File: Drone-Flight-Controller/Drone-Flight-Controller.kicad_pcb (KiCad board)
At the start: 2 copper layers, 30 x 65 mm, 45 parts, among them J1 Screw_Terminal_01x02, J10 TestPoint, J11 TestPoint, J12 TestPoint, J2 Raspberry_Pi_4, J3 TestPoint, J4 TestPoint, J5 TestPoint, J6 TestPoint, J7 TestPoint, J8 TestPoint, J9 TestPoint, SW1 SW_Omron_B3FS, U1 MCP1700x-180xxMB, U2 LMR51430, U3 ADC101C021CIMK, U4 ICM-20948, U5 BMP280, U6 PCA9531PW

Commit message: move imu to center of pcb
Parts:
- moved U4 7.45 mm to (27.2, 44.6)
- moved C2 7.15 mm to (23.6, 38.6)
- moved C3 7.15 mm to (23.6, 40.6)
- moved U1 7.15 mm to (27.0, 39.6)
- moved C7 7.07 mm to (25.0, 47.8), turned to -90 degrees
- moved C6 6.61 mm to (24.0, 43.2)
- moved C9 6.61 mm to (24.0, 47.2)
- moved R7 6.61 mm to (24.0, 45.2)
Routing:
- net +5V: track 73.4 -> 39.9 mm, vias 11 -> 18
- net +3.3V: track 79.4 -> 61.8 mm
- net +1V8: track 10.8 -> 4.61 mm
- net GND: track 5.39 -> 1.42 mm, vias 17 -> 14
- net I2C_SCL: track 75.3 -> 77.9 mm, vias 3 -> 5
- net I2C_SDA: track 74.2 -> 76.0 mm
- net Net-(U4-REGOUT): track 1.77 -> 2.79 mm
- net Net-(U4-SDO/AD0): track 1.47 -> 2.47 mm
- added copper zone on F.Cu, net +3.3V
- added copper zone on B.Cu, net +5V
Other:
- board text added: "DO NOT COVER"
- board text added: "imu"
- board text removed: "gyro"

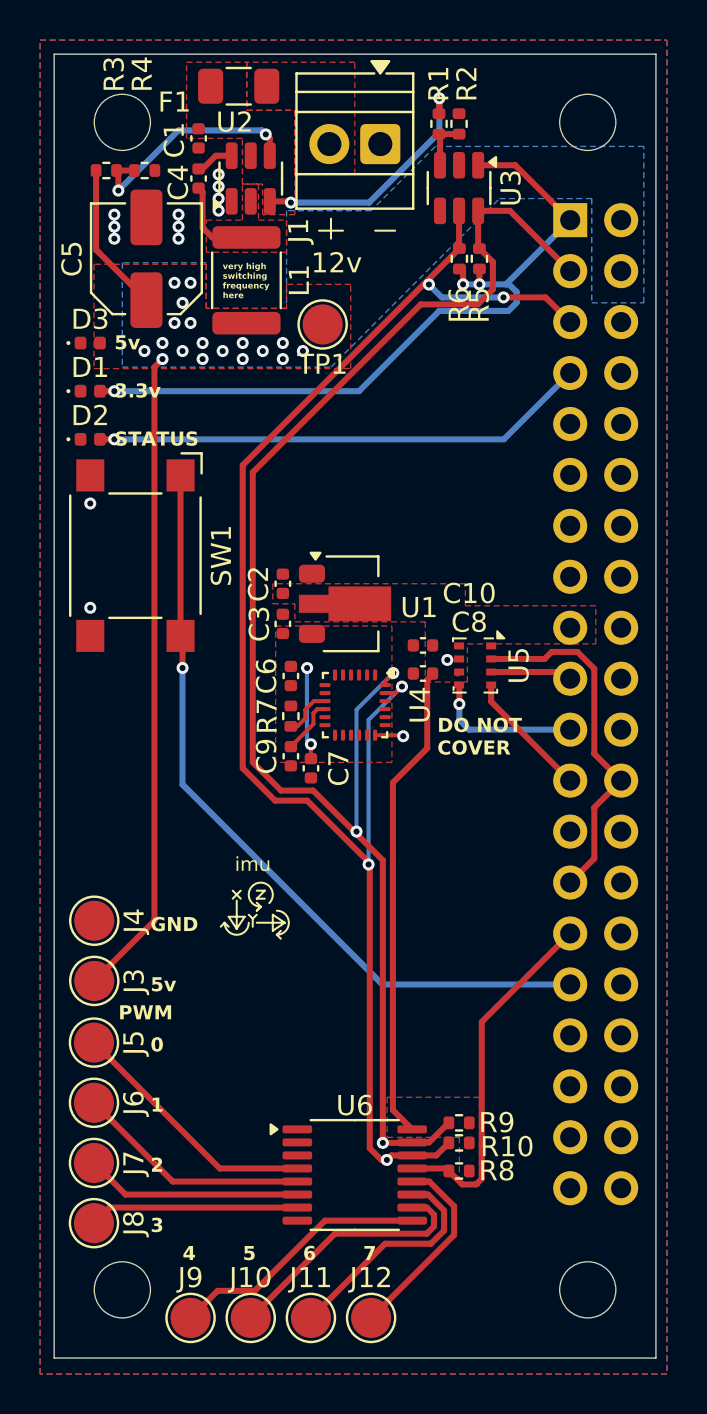
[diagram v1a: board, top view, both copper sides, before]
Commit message: added imu level shifter
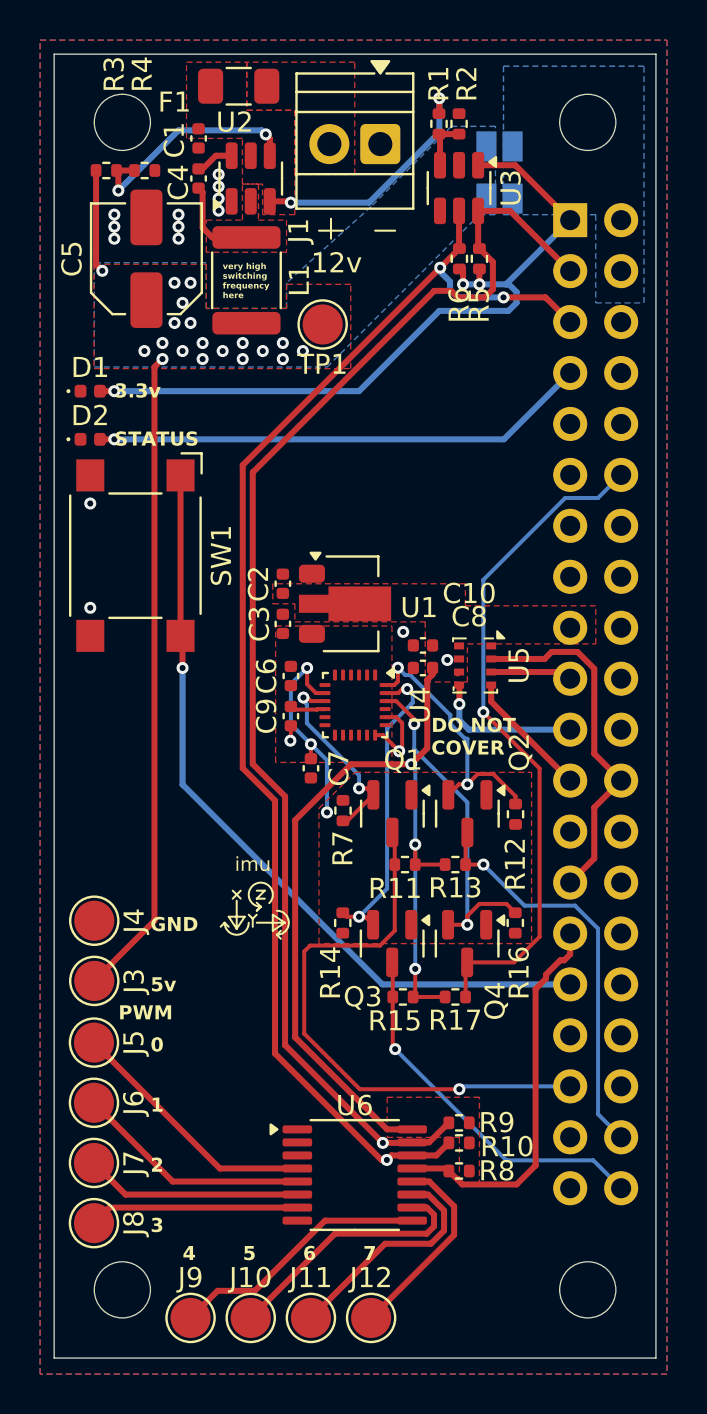
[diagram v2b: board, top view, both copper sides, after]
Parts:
- removed D3: LED, LED_SMD:LED_0402_1005Metric
- added JP1: SolderJumper_2_Open, Jumper:SolderJumper-2_P1.3mm_Open_Pad1.0x1.5mm, B.Cu at (34.4, 16.8)
- added JP2: SolderJumper_2_Open, Jumper:SolderJumper-2_P1.3mm_Open_Pad1.0x1.5mm, B.Cu at (34.4, 19.4)
- added Q1: BSS138, Package_TO_SOT_SMD:SOT-23, F.Cu at (29.1, 50.1)
- added Q2: BSS138, Package_TO_SOT_SMD:SOT-23, F.Cu at (32.8, 50.1)
- added Q3: BSS138, Package_TO_SOT_SMD:SOT-23, F.Cu at (29.1, 56.5)
- added Q4: BSS138, Package_TO_SOT_SMD:SOT-23, F.Cu at (32.8, 56.5)
- added R11: 10kOhm, Resistor_SMD:R_0402_1005Metric, F.Cu at (29.7, 52.6)
- added R12: 10kOhm, Resistor_SMD:R_0402_1005Metric, F.Cu at (35.2, 50.1)
- added R13: 10kOhm, Resistor_SMD:R_0402_1005Metric, F.Cu at (32.2, 52.6)
- added R14: 10kOhm, Resistor_SMD:R_0402_1005Metric, F.Cu at (26.6, 55.5)
- added R15: 10kOhm, Resistor_SMD:R_0402_1005Metric, F.Cu at (29.6, 59.2)
- added R16: 10kOhm, Resistor_SMD:R_0402_1005Metric, F.Cu at (35.2, 55.5)
- added R17: 10kOhm, Resistor_SMD:R_0402_1005Metric, F.Cu at (32.2, 59.2)
- moved R7 5.38 mm to (26.6, 49.9)
- moved C9 2.00 mm to (24.0, 45.2)
- moved C8 0.28 mm to (30.6, 42.8)
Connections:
- net Net-(U4-SDO/AD0) renamed IMU_SDO_LV
- J2 pad 12: unconnected-(J2-GPIO18/SPI1_~{CE0}/PCM_CLK/PWM0-Pad12) -> IMU_CS_HV
- J2 pad 35: unconnected-(J2-GPIO19/SPI1_MISO/PCM_FS-Pad35) -> IMU_SDO_HV
- J2 pad 38: unconnected-(J2-GPIO20/SPI1_MOSI/PCM_DIN/PWM1-Pad38) -> IMU_SDI_HV
- J2 pad 40: unconnected-(J2-GPIO21/SPI1_SCLK/PCM_DOUT-Pad40) -> IMU_SCL_HV
- U4 pad 22: unconnected-(U4-~{CS}-Pad22) -> IMU_CS_LV
- U4 pad 23: I2C_SCL -> IMU_SCL_LV
- U4 pad 24: I2C_SDA -> IMU_SDI_LV
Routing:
- net IMU_CS_HV: track 0.00 -> 33.9 mm, vias 0 -> 1
- net IMU_SDO_HV: track 0.00 -> 28.5 mm, vias 0 -> 1
- net +3.3V: track 61.8 -> 84.2 mm, vias 3 -> 6
- net IMU_SDI_HV: track 0.00 -> 20.4 mm, vias 0 -> 1
- net IMU_SCL_HV: track 0.00 -> 18.5 mm, vias 0 -> 1
- net IMU_CS_LV: track 0.00 -> 17.4 mm, vias 0 -> 2
- net IMU_SCL_LV: track 0.00 -> 15.6 mm, vias 0 -> 2
- net IMU_SDI_LV: track 0.00 -> 13.5 mm, vias 0 -> 2
- net I2C_SCL: track 77.9 -> 66.5 mm, vias 5 -> 3
- net I2C_SDA: track 76.0 -> 65.9 mm, vias 3 -> 1
- net IMU_SDO_LV: track 2.47 -> 9.72 mm, vias 0 -> 2
- net +1V8: track 4.61 -> 10.9 mm, vias 2 -> 3
- net GND: track 1.42 -> 4.72 mm, vias 14 -> 16
- net +5V: track 39.9 -> 37.5 mm, vias 18 -> 19
- net PWM_RESET: track 18.0 -> 19.3 mm
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
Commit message: optimized routing
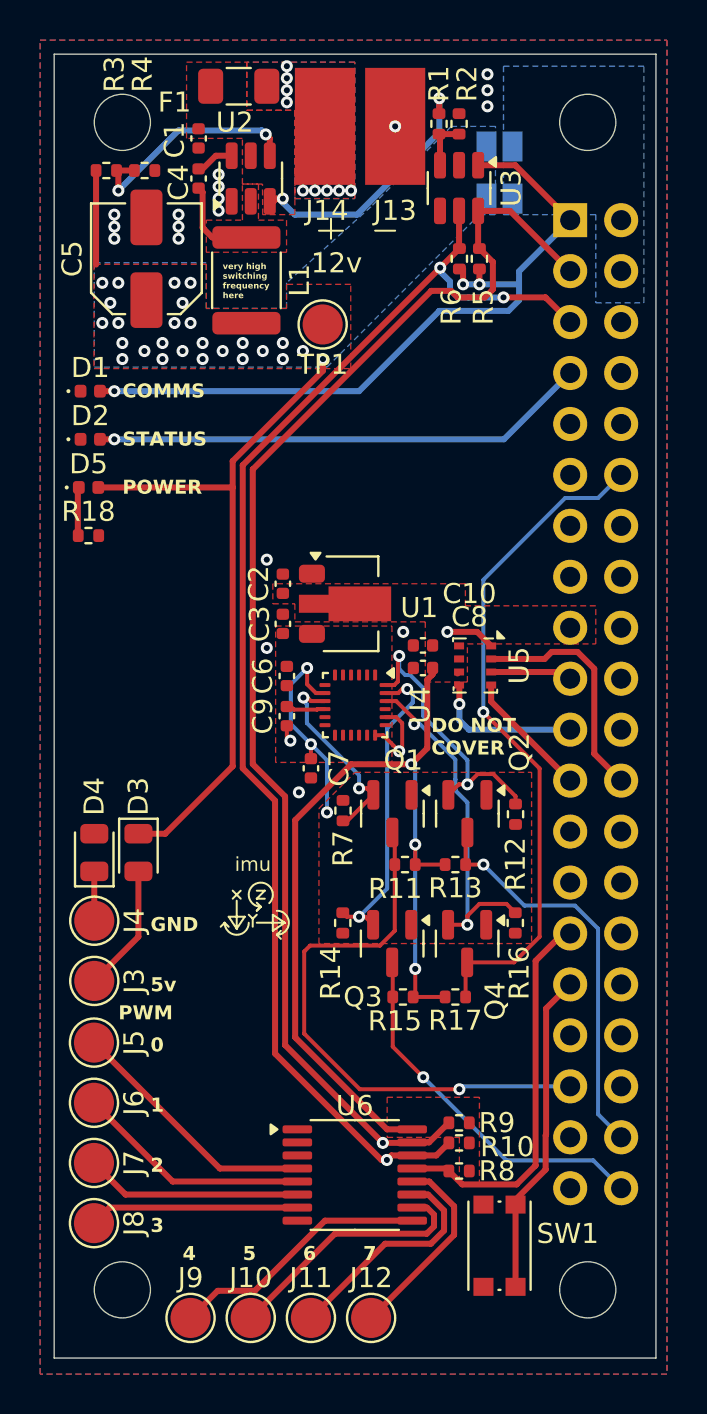
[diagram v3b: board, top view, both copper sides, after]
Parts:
- removed J1: Screw_Terminal_01x02, TerminalBlock:TerminalBlock_Xinya_XY308-2.54-2P_1x02_P2.54mm_Horizontal
- added D3: D, Diode_SMD:D_0805_2012Metric, F.Cu at (16.4, 52.0)
- added D4: D, Diode_SMD:D_0805_2012Metric, F.Cu at (14.2, 52.0)
- added D5: LED, LED_SMD:LED_0402_1005Metric, F.Cu at (13.9, 33.8)
- added J13: TestPoint, TestPoint:TestPoint_Pad_D2.0mm, F.Cu at (29.2, 12.8)
- added J14: TestPoint, TestPoint:TestPoint_Pad_D2.0mm, F.Cu at (25.8, 18.7)
- added R18: 85Ohm, Resistor_SMD:R_0402_1005Metric, F.Cu at (13.9, 36.2)
- SW1: footprint Button_Switch_SMD:SW_SPST_Omron_B3FS-100xP -> Button_Switch_SMD:SW_Push_1P1T_NO_CK_KMR2
- moved SW1 38.9 mm to (34.4, 71.6)
- moved C6 0.20 mm to (23.8, 43.2)
- moved C9 0.20 mm to (23.8, 45.2)
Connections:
- J3 pad 1: +5V -> Net-(D3-A)
- J4 pad 1: GND -> Net-(D4-K)
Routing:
- net Net-(J2-GPCLK2/GPIO06): track 38.9 -> 16.2 mm, vias 1 -> 0
- net Net-(D3-A): track 0.00 -> 6.37 mm
- net BAROMETER_CSB: track 17.9 -> 11.8 mm
- net Net-(D4-K): track 0.00 -> 2.46 mm
- net Net-(D5-K): track 0.00 -> 2.35 mm
- net GND: track 4.72 -> 7.06 mm, vias 16 -> 21
- net +5V: track 37.5 -> 39.6 mm, vias 19 -> 26
- net IMU_SDI_LV: track 13.5 -> 14.6 mm
- net +12V: track 12.4 -> 13.1 mm
- net Net-(F1-Pad1): vias 0 -> 9
- added copper zone on B.Cu, net Net-(F1-Pad1)
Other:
- board text added: "COMMS"
- board text added: "POWER"
- board text removed: "3.3v"

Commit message: connect imu and barometer to spi0
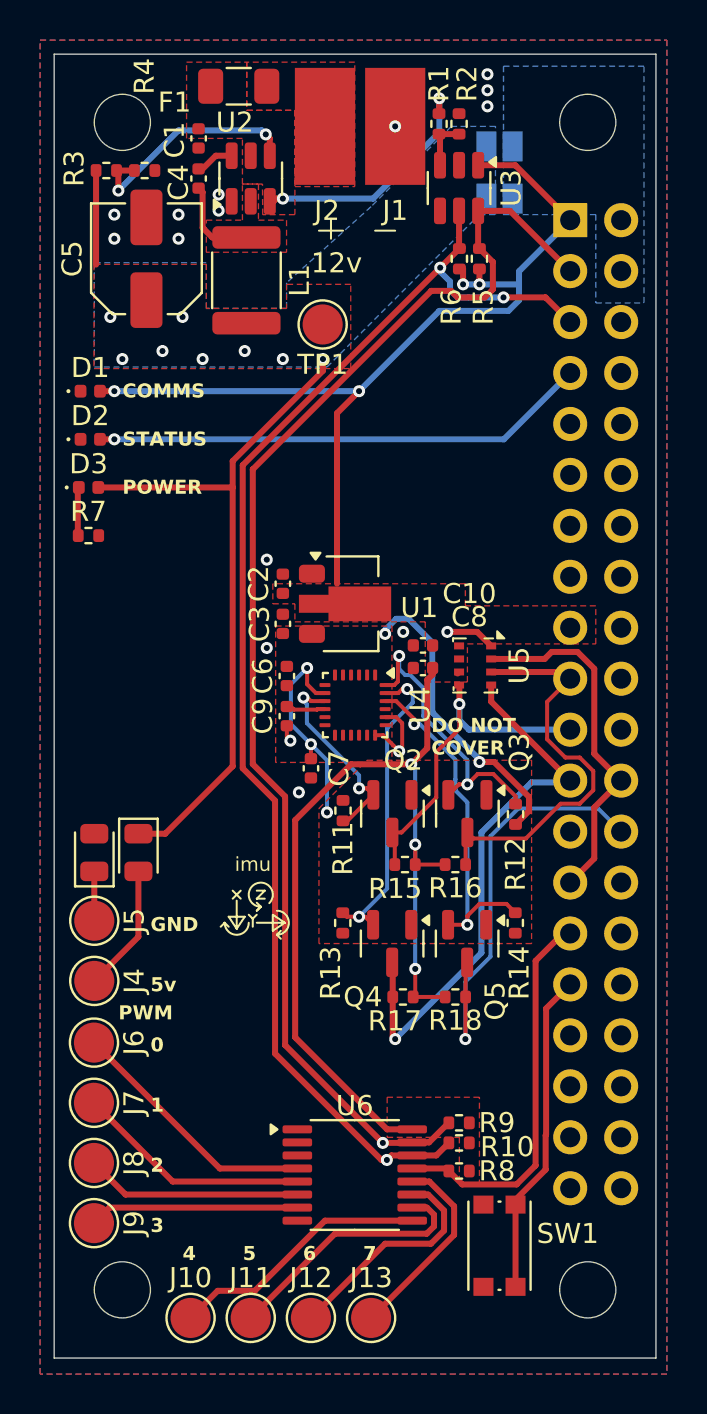
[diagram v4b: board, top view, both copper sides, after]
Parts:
- F1: value Fuse -> 2A
- renumbered D5 to D3, D3 to D4, D4 to D5, J13 to J1, J9 to J10, J10 to J11, J11 to J12, J12 to J13, J14 to J2, J2 to J3, J3 to J4, J4 to J5, J5 to J6, J6 to J7, J7 to J8, J8 to J9, Q1 to Q2, Q2 to Q3, Q3 to Q4, Q4 to Q5, R7 to R11, R14 to R13, R16 to R14, R11 to R15, R13 to R16, R15 to R17, R17 to R18, R18 to R7
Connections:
- net IMU_SCL_LV renamed SPI0_SCL_LV
- net IMU_SDI_LV renamed SPI0_SDI_LV
- net IMU_SDO_LV renamed SPI0_SDO_LV
- J3 pad 12: IMU_CS_HV -> unconnected-(J3-GPIO18/SPI1_~{CE0}/PCM_CLK/PWM0-Pad12)
- J3 pad 19: BAROMETER_SDI -> SPI0_MOSI
- J3 pad 21: BAROMETER_SDO -> SPI0_MISO
- J3 pad 23: BAROMETER_SCK -> SPI0_SCLK
- J3 pad 26: unconnected-(J2-~{CE1}_SPI0/GPIO07-Pad26) -> IMU_CS_HV
- J3 pad 35: IMU_SDO_HV -> unconnected-(J3-GPIO19/SPI1_MISO/PCM_FS-Pad35)
- J3 pad 38: IMU_SDI_HV -> unconnected-(J3-GPIO20/SPI1_MOSI/PCM_DIN/PWM1-Pad38)
- J3 pad 40: IMU_SCL_HV -> unconnected-(J3-GPIO21/SPI1_SCLK/PCM_DOUT-Pad40)
- Q2 pad 3: IMU_SDO_HV -> SPI0_MISO
- Q3 pad 3: IMU_SDI_HV -> SPI0_MOSI
- Q4 pad 3: IMU_SCL_HV -> SPI0_SCLK
- R15 pad 1: IMU_SDO_HV -> SPI0_MISO
- R16 pad 1: IMU_SDI_HV -> SPI0_MOSI
- R17 pad 1: IMU_SCL_HV -> SPI0_SCLK
- U5 pad 3: BAROMETER_SDI -> SPI0_MOSI
- U5 pad 4: BAROMETER_SCK -> SPI0_SCLK
- U5 pad 5: BAROMETER_SDO -> SPI0_MISO
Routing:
- net IMU_SDO_HV: track 28.5 -> 0.00 mm, vias 1 -> 0
- net SPI0_SCLK: track 0.00 -> 28.0 mm, vias 0 -> 1
- net SPI0_MOSI: track 0.00 -> 20.5 mm
- net IMU_SDI_HV: track 20.4 -> 0.00 mm, vias 1 -> 0
- net IMU_SCL_HV: track 18.5 -> 0.00 mm, vias 1 -> 0
- net SPI0_MISO: track 0.00 -> 17.2 mm, vias 0 -> 1
- net +1V8: track 10.9 -> 25.9 mm, vias 3 -> 5
- net IMU_CS_HV: track 33.9 -> 22.1 mm
- net +3.3V: track 84.4 -> 94.4 mm, vias 6 -> 7
- net BAROMETER_SDO: track 7.48 -> 0.00 mm, vias 1 -> 0
- net BAROMETER_SCK: track 6.55 -> 0.00 mm
- net BAROMETER_CSB: track 11.8 -> 17.9 mm
- net BAROMETER_SDI: track 4.08 -> 0.00 mm
- net +12V: track 13.1 -> 12.3 mm
- net Net-(F1-Pad1): vias 9 -> 0
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- removed copper zone on B.Cu, net Net-(F1-Pad1)
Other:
- board text removed: "very high switching frequency here"

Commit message: switch to bmp390 for barometer
bmp280 isnt being stocked at digikey or mouser anymore
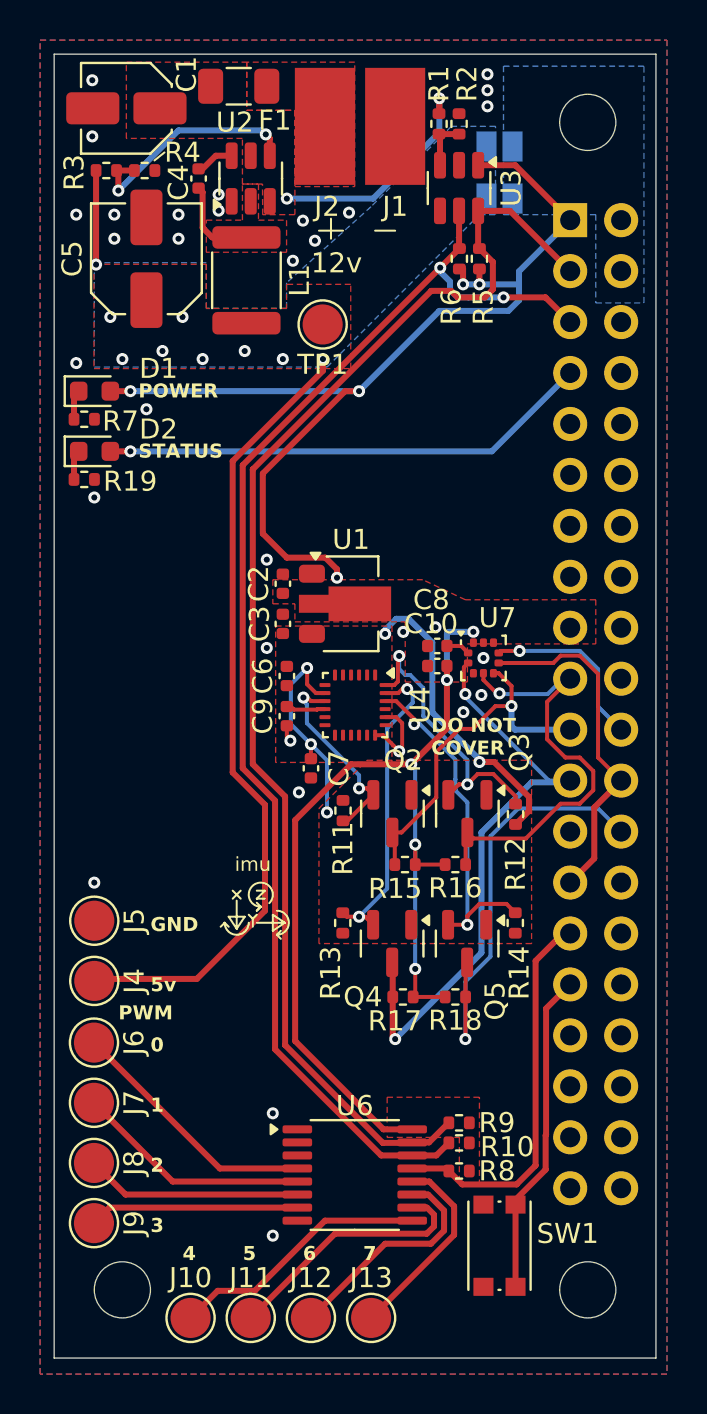
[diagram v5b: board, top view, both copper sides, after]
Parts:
- removed D3: LED, LED_SMD:LED_0402_1005Metric
- removed D4, D5: D, Diode_SMD:D_0805_2012Metric
- removed U5: BMP280, Package_LGA:Bosch_LGA-8_2x2.5mm_P0.65mm_ClockwisePinNumbering
- added R19: CRCW040268R0FKTD, Resistor_SMD:R_0402_1005Metric, F.Cu at (13.7, 33.4)
- added U7: BMP390, Package_LGA:ST_HLGA-10_2x2mm_P0.5mm_LayoutBorder3x2y, F.Cu at (33.6, 42.3)
- C1: value 2.2uF 35v -> UWG1V2R2MCL1GB; footprint Capacitor_SMD:C_0402_1005Metric -> Capacitor_SMD:C_Elec_4x5.4
- C10, C8: value 100nF -> CL05B104KP5VPNC
- C2, C3: value 1uF -> CGA2B1X7T0G105M050BC
- C4, C6, C7, C9: value 0.1uF -> C1005X5R1C104K050BA
- C5: value 33uF -> UWG1A330MCL1GB
- D1, D2: value LED -> SML-D12U1WT86; footprint LED_SMD:LED_0402_1005Metric -> LED_SMD:LED_0603_1608Metric
- F1: value 2A -> JB12F2001R
- J3: value Raspberry_Pi_4 -> 2044-2X20G00RA
- L1: value 6.8uH -> ASPI-6045S-6R8M-T
- R1: value 1.5kOhm -> CRCW02011K50FNEDAT
- R10, R11, R12, R13, R14, R15, R16, R17, R18, R5, R6, R8, R9: value 10kOhm -> RK73G1ERTTP1002F
- R2: value 1kOhm -> CRCW02011K00JNEDAT
- R3: value 100kOhm -> ERJ-S02J104X
- R4: value 13.7kOhm -> ERA-2APB1372X
- R7: value 85Ohm -> CRCW040268R0FKTD
- SW1: value SW_Omron_B3FS -> TL3301NF160QG-KR
- U1: value MCP1700x-180xxMB -> MCP1700T-1802E/MB
- moved R7 5.80 mm to (13.7, 30.4)
- moved C1 3.90 mm to (15.8, 14.9), turned to 180 degrees
- moved C8 1.31 mm to (31.3, 41.7)
- moved C10 1.25 mm to (31.3, 42.7)
- moved D2 0.64 mm to (14.2, 32.0)
- moved D1 0.21 mm to (14.2, 29.0)
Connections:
- C8 pad 1: +3.3V -> Net-(U7-VDDIO)
- D1 pad 1: GND -> Net-(D1-K)
- D2 pad 1: GND -> Net-(D2-K)
- J3 pad 22: unconnected-(J3-GPIO25/SDIO_DAT1-Pad22) -> BAROMETER_INT
- J4 pad 1: Net-(D4-A) -> +5V
- J5 pad 1: Net-(D5-K) -> GND
- R7 pad 1: Net-(D3-K) -> Net-(D1-K)
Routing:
- net BAROMETER_INT: track 0.00 -> 8.86 mm, vias 0 -> 1
- net +3.3V: track 94.4 -> 102.6 mm, vias 7 -> 10
- net Net-(D4-A): track 6.37 -> 0.00 mm
- net +5V: track 39.6 -> 44.5 mm, vias 8 -> 9
- net GND: track 7.06 -> 4.58 mm, vias 17 -> 32
- net Net-(D5-K): track 2.46 -> 0.00 mm
- net SPI0_SCLK: track 28.0 -> 30.4 mm, vias 1 -> 2
- net Net-(D3-K): track 2.35 -> 0.00 mm
- net SPI0_MOSI: track 20.5 -> 22.2 mm, vias 0 -> 1
- net Net-(D2-K): track 0.00 -> 1.50 mm
- net Net-(D1-K): track 0.00 -> 1.50 mm
- net Net-(U7-VDDIO): track 0.00 -> 1.20 mm
- net +12V: track 12.3 -> 11.4 mm
- net SPI0_MISO: track 17.2 -> 17.7 mm
- net I2C_SCL: track 66.5 -> 66.2 mm, vias 3 -> 2
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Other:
- outline, holes or cut-outs redrawn
- board text removed: "COMMS"
